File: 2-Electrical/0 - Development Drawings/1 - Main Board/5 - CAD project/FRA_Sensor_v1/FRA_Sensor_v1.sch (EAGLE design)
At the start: 213 parts, among them IC1 CP2101, IC2 ADS1115IDGSR, IC3 P82B715DR, IC4 ADS1115IDGSR, IC5 ADS1115IDGSR, IC8 PCA9555PW, IC9 LDK320ADU50R, J2 ETH_CONN, J3 PJ-059A, J5 WM9734TR-ND, J8 1140084168, J9 + G SCL SDA, Q10 FDN306P, Q11 FDN306P, Q12 FDN306P, Q13 FDN306P, Q14 FDN306P, Q15 FDN306P, Q2 FDN306P, Q3 Si2300DS, Q5 FDN306P, Q6 FDN306P, Q7 DNI, Q8 FDN306P, Q9 FDN306P, T1 BC847, T2 BC847, U1 PCA9509DP, U2 ESP-WROOM-32, X1 TB001-500-02BE, Y3 32.768kHz

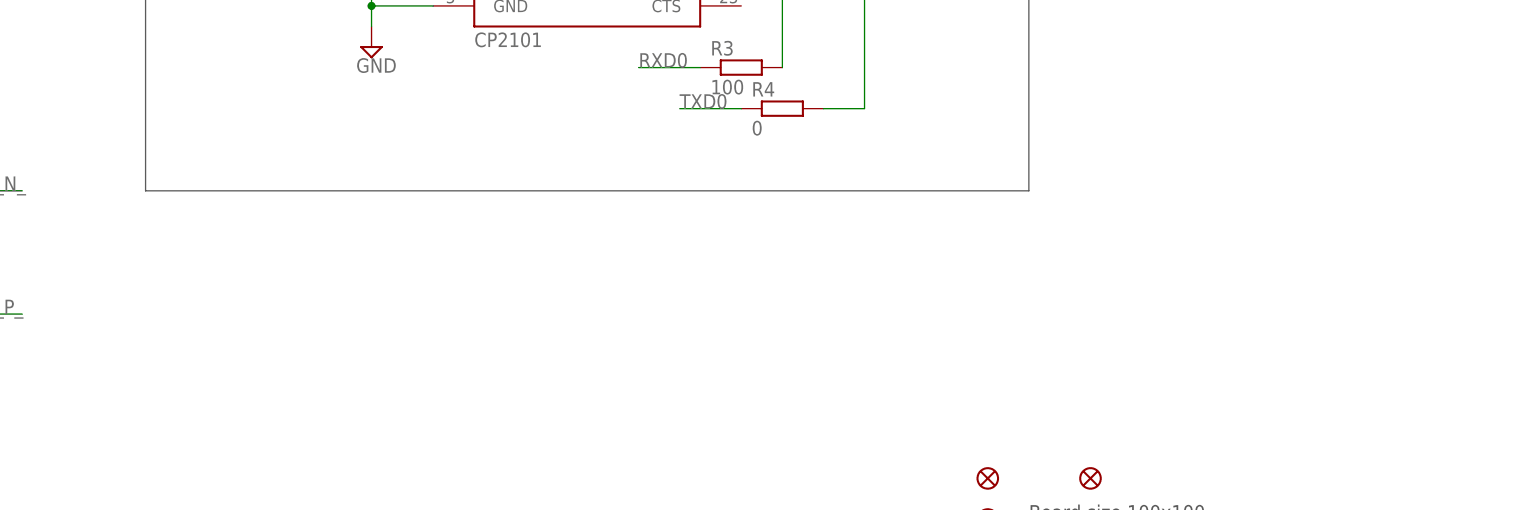
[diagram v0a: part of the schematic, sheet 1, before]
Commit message: fixed network, ADC begin
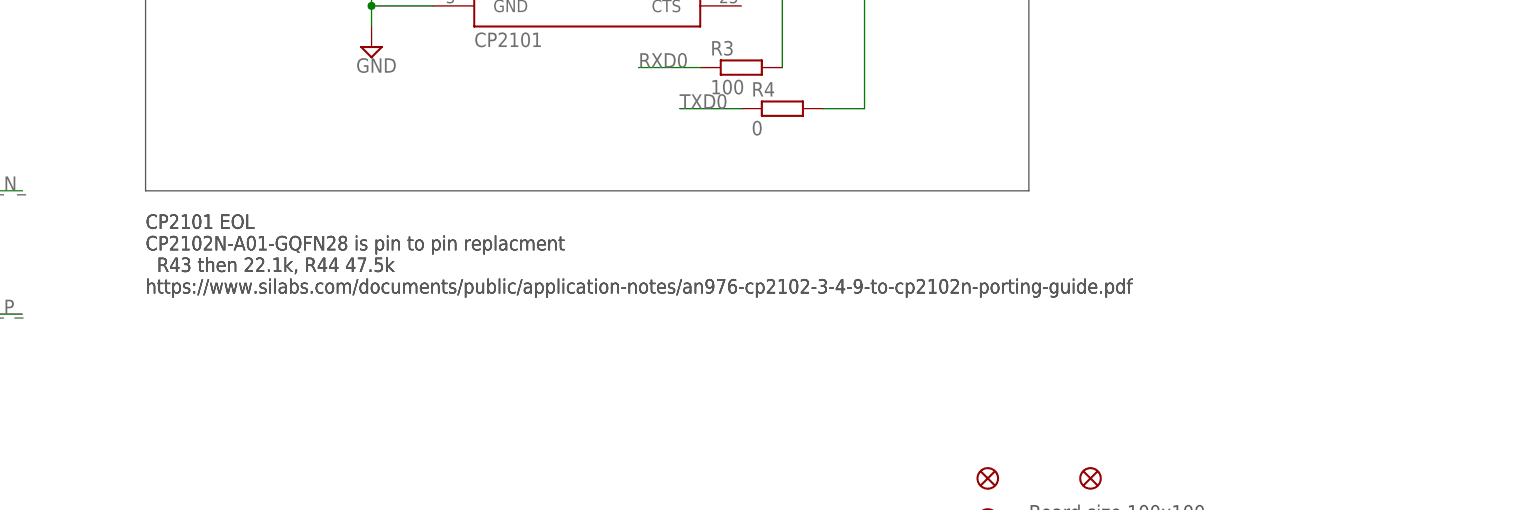
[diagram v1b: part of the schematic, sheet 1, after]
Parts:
- C10: PARTNO (none) -> GRM188R61E106KA73J
- C17: PARTNO (none) -> GRM188R61A106KE69J
- FAN_5V: value FAN -> 2pin; PARTNO 640456-2 -> TSW-102-07-G-S
- J3: PARTNO PJ-031C -> PJ-059A
- J4: value (none) -> DNI
- J5: PARTNO Molex 105133-0001 -> 105133-0001
- J9: value + G SCL SDA -> 4pin
- L2, L3: PARTNO SRN6045TA-1R5Y -> SRP5030CA-1R5M
- LED_HDR: PARTNO 640456-2 -> TSW-102-07-G-S
- U$1, U$4: PARTNO TPS563249DDCR -> TPS563249DDCR
- U$10, U$11, U$12, U$13, U$14, U$15, U$16, U$3, U$8, U$9: PARTNO Wurth 61200621621 -> 61200621621
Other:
- note added: "CP2101 EOL CP2102N-A01-GQFN28 is pin to pin replacment R43 then 22.1k, R44 47.5k https://www.silabs.com/documents/public/application-notes/an976-cp2102-3-4-9-to-cp2102n-porting-guide.pdf"
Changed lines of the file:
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@@
 <attributes>
 <attribute name="CNAME" value="FRA Sensor Unit"/>
-<attribute name="CREVISION" value="02"/>
+<attribute name="CREVISION" value="03"/>
 </attributes>
 <variantdefs>
@@
 <attribute name="PARTNO" value="CES-106-01-T-D"/>
 </part>
-<part name="J4" library="sd-mmc" deviceset="SDCARD" device="">
+<part name="J4" library="sd-mmc" deviceset="SDCARD" device="" value="DNI">
 <attribute name="PARTNO" value="GSD090012SEU"/>
 </part>
 <part name="U$4" library="FRA_eagle_lib" deviceset="TPS5632149DDCR" device="" value="TPS563249DDCR">
-<attribute name="PARTNO" value="TPS563249DDCR"/>
+<attribute name="PARTNO" value="TPS563249DDCR
+"/>
 </part>
 <part name="SUPPLY6" library="supply2" deviceset="GND" device=""/>
@@
 <part name="SUPPLY14" library="supply2" deviceset="GND" device=""/>
 <part name="SUPPLY15" library="supply2" deviceset="GND" device=""/>
-<part name="C10" library="resistor" deviceset="C-EU" device="C0603K" value="10u/25V"/>
+<part name="C10" library="resistor" deviceset="C-EU" device="C0603K" value="10u/25V">
+<attribute name="PARTNO" value="GRM188R61E106KA73J"/>
+</part>
 <part name="SUPPLY21" library="supply2" deviceset="GND" device=""/>
 <part name="SUPPLY22" library="supply2" deviceset="GND" device=""/>
@@
 <part name="SUPPLY30" library="SparkFun-PowerSymbols" deviceset="3.3V" device=""/>
 <part name="L2" library="FRA_eagle_lib" deviceset="SRP5030CA-1R5M" device="" value="SRP5030CA-1R5M">
-<attribute name="PARTNO" value="SRN6045TA-1R5Y"/>
+<attribute name="PARTNO" value="SRP5030CA-1R5M
+"/>
 </part>
 <part name="Q2" library="microbuilder" deviceset="MOSFET-P" device="WIDE" value="FDN306P">
@@
 <part name="SUPPLY49" library="SparkFun-PowerSymbols" deviceset="V_USB" device=""/>
 <part name="U$1" library="FRA_eagle_lib" deviceset="TPS5632149DDCR" device="" value="TPS563249DDCR">
-<attribute name="PARTNO" value="TPS563249DDCR"/>
+<attribute name="PARTNO" value="TPS563249DDCR
+"/>
 </part>
 <part name="SUPPLY11" library="supply2" deviceset="GND" device=""/>
@@
 <part name="SUPPLY55" library="supply2" deviceset="GND" device=""/>
 <part name="SUPPLY60" library="supply2" deviceset="GND" device=""/>
-<part name="C17" library="resistor" deviceset="C-EU" device="C0603K" value="10u"/>
+<part name="C17" library="resistor" deviceset="C-EU" device="C0603K" value="10u">
+<attribute name="PARTNO" value="GRM188R61A106KE69J"/>
+</part>
 <part name="SUPPLY62" library="supply2" deviceset="GND" device=""/>
 <part name="SUPPLY63" library="supply2" deviceset="GND" device=""/>
@@
 </part>
 <part name="L3" library="FRA_eagle_lib" deviceset="SRP5030CA-1R5M" device="" value="SRP5030CA-1R5M">
-<attribute name="PARTNO" value="SRN6045TA-1R5Y"/>
+<attribute name="PARTNO" value="SRP5030CA-1R5M
+"/>
 </part>
 <part name="R53" library="resistor" deviceset="R-EU_" device="R0603" value="100k">
@@
 </part>
 <part name="J5" library="SparkFun-Connectors" deviceset="USB_MICRO-B" device="_FEMALE-SMT-VERT" value="WM9734TR-ND ">
-<attribute name="PARTNO" value="Molex 105133-0001"/>
+<attribute name="PARTNO" value="105133-0001"/>
 </part>
 <part name="SUPPLY68" library="SparkFun-PowerSymbols" deviceset="V_USB" device=""/>
@@
 </part>
 <part name="SUPPLY19" library="supply2" deviceset="GND" device=""/>
-<part name="FAN_5V" library="pinhead" deviceset="PINHD-1X2" device="" value="FAN">
-<attribute name="PARTNO" value="640456-2"/>
+<part name="FAN_5V" library="pinhead" deviceset="PINHD-1X2" device="" value="2pin">
+<attribute name="PARTNO" value="TSW-102-07-G-S"/>
 </part>
 <part name="SUPPLY87" library="SparkFun-PowerSymbols" deviceset="5V" device=""/>
@@
 <part name="SUPPLY121" library="SparkFun-PowerSymbols" deviceset="3.3V" device=""/>
 <part name="U$3" library="FRA_eagle_lib" deviceset="CONN_03X2_WE_61200621621" device="">
-<attribute name="PARTNO" value="Wurth 61200621621"/>
+<attribute name="PARTNO" value="61200621621"/>
 </part>
 <part name="SUPPLY59" library="supply2" deviceset="AGND" device=""/>
@@
 </part>
 <part name="U$8" library="FRA_eagle_lib" deviceset="CONN_03X2_WE_61200621621" device="">
-<attribute name="PARTNO" value="Wurth 61200621621"/>
+<attribute name="PARTNO" value="61200621621"/>
 </part>
 <part name="SUPPLY58" library="supply2" deviceset="AGND" device=""/>
@@
 </part>
 <part name="U$9" library="FRA_eagle_lib" deviceset="CONN_03X2_WE_61200621621" device="">
-<attribute name="PARTNO" value="Wurth 61200621621"/>
+<attribute name="PARTNO" value="61200621621"/>
 </part>
 <part name="SUPPLY108" library="supply2" deviceset="AGND" device=""/>
@@
 </part>
 <part name="U$10" library="FRA_eagle_lib" deviceset="CONN_03X2_WE_61200621621" device="">
-<attribute name="PARTNO" value="Wurth 61200621621"/>
+<attribute name="PARTNO" value="61200621621"/>
 </part>
 <part name="SUPPLY116" library="supply2" deviceset="AGND" device=""/>
@@
 </part>
 <part name="U$11" library="FRA_eagle_lib" deviceset="CONN_03X2_WE_61200621621" device="">
-<attribute name="PARTNO" value="Wurth 61200621621"/>
+<attribute name="PARTNO" value="61200621621"/>
 </part>
 <part name="SUPPLY124" library="supply2" deviceset="AGND" device=""/>
@@
 </part>
 <part name="U$12" library="FRA_eagle_lib" deviceset="CONN_03X2_WE_61200621621" device="">
-<attribute name="PARTNO" value="Wurth 61200621621"/>
+<attribute name="PARTNO" value="61200621621"/>
 </part>
 <part name="SUPPLY126" library="supply2" deviceset="AGND" device=""/>
@@
 <part name="FRAME7" library="SparkFun-Aesthetics" deviceset="FRAME-A4L" device=""/>
 <part name="U$13" library="FRA_eagle_lib" deviceset="CONN_03X2_WE_61200621621" device="">
-<attribute name="PARTNO" value="Wurth 61200621621"/>
+<attribute name="PARTNO" value="61200621621"/>
 </part>
 <part name="SUPPLY70" library="supply2" deviceset="AGND" device=""/>
@@
 </part>
 <part name="U$14" library="FRA_eagle_lib" deviceset="CONN_03X2_WE_61200621621" device="">
-<attribute name="PARTNO" value="Wurth 61200621621"/>
+<attribute name="PARTNO" value="61200621621"/>
 </part>
 <part name="SUPPLY85" library="supply2" deviceset="AGND" device=""/>
@@
 </part>
 <part name="U$15" library="FRA_eagle_lib" deviceset="CONN_03X2_WE_61200621621" device="">
-<attribute name="PARTNO" value="Wurth 61200621621"/>
+<attribute name="PARTNO" value="61200621621"/>
 </part>
 <part name="SUPPLY129" library="supply2" deviceset="AGND" device=""/>
@@
 </part>
 <part name="U$16" library="FRA_eagle_lib" deviceset="CONN_03X2_WE_61200621621" device="">
-<attribute name="PARTNO" value="Wurth 61200621621"/>
+<attribute name="PARTNO" value="61200621621"/>
 </part>
 <part name="SUPPLY131" library="supply2" deviceset="AGND" device=""/>
@@
 </part>
 <part name="SUPPLY66" library="supply2" deviceset="AGND" device=""/>
-<part name="J9" library="pinhead" deviceset="PINHD-1X4" device="" value="+  G  SCL SDA">
+<part name="J9" library="pinhead" deviceset="PINHD-1X4" device="" value="4pin">
 <attribute name="PARTNO" value="61300411121"/>
 </part>
@@
 <part name="SUPPLY96" library="supply2" deviceset="+5V/1" device="" value="5V_F"/>
 <part name="J3" library="FRA_eagle_lib" deviceset="PJ-059A" device="">
-<attribute name="PARTNO" value="PJ-031C"/>
+<attribute name="PARTNO" value="PJ-059A "/>
 </part>
 <part name="FB10" library="microbuilder" deviceset="FERRITE" device="">
@@
 <part name="SUPPLY132" library="SparkFun-PowerSymbols" deviceset="5V" device=""/>
 <part name="LED_HDR" library="pinhead" deviceset="PINHD-1X2" device="" value="2pin">
-<attribute name="PARTNO" value="640456-2"/>
+<attribute name="PARTNO" value="TSW-102-07-G-S"/>
 </part>
 </parts>
@@
 <text x="58.42" y="86.36" size="1.778" layer="97">Molex
 105133-0001</text>
+<text x="142.24" y="55.88" size="1.778" layer="97">CP2101 EOL
+CP2102N-A01-GQFN28 is pin to pin replacment
+  R43 then 22.1k, R44 47.5k
+https://www.silabs.com/documents/public/application-notes/an976-cp2102-3-4-9-to-cp2102n-porting-guide.pdf</text>
+<text x="142.24" y="55.88" size="1.778" layer="97">CP2101 EOL
+CP2102N-A01-GQFN28 is pin to pin replacment
+  R43 then 22.1k, R44 47.5k
+https://www.silabs.com/documents/public/application-notes/an976-cp2102-3-4-9-to-cp2102n-porting-guide.pdf</text>
 </plain>
 <instances>
@@
 <instance part="SUPPLY14" gate="GND" x="101.6" y="127"/>
 <instance part="SUPPLY15" gate="GND" x="88.9" y="127"/>
-<instance part="C10" gate="G$1" x="160.02" y="119.38"/>
+<instance part="C10" gate="G$1" x="160.02" y="119.38">
+<attribute name="PARTNO" x="160.02" y="119.38" size="1.778" layer="96" display="off"/>
+</instance>
 <instance part="SUPPLY21" gate="GND" x="160.02" y="111.76"/>
 <instance part="SUPPLY22" gate="GND" x="170.18" y="111.76"/>
@@
 <instance part="SUPPLY55" gate="GND" x="101.6" y="55.88"/>
 <instance part="SUPPLY60" gate="GND" x="88.9" y="55.88"/>
-<instance part="C17" gate="G$1" x="160.02" y="48.26"/>
+<instance part="C17" gate="G$1" x="160.02" y="48.26">
+<attribute name="PARTNO" x="160.02" y="48.26" size="1.778" layer="96" display="off"/>
+</instance>
 <instance part="SUPPLY62" gate="GND" x="160.02" y="40.64"/>
 <instance part="SUPPLY63" gate="GND" x="170.18" y="40.64"/>

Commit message: sch main final touches
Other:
- note added: "Man. PN may be wrong (TH not SMT)"
- note added: "place on BOT in schematics. placed on top in assembly"
- note removed: "place on BOT"
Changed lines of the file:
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@@
 </part>
 <part name="U$4" library="FRA_eagle_lib" deviceset="TPS5632149DDCR" device="" value="TPS563249DDCR">
-<attribute name="PARTNO" value="TPS563249DDCR
-"/>
+<attribute name="PARTNO" value="TPS563249DDCR "/>
 </part>
 <part name="SUPPLY6" library="supply2" deviceset="GND" device=""/>
@@
 <part name="SUPPLY30" library="SparkFun-PowerSymbols" deviceset="3.3V" device=""/>
 <part name="L2" library="FRA_eagle_lib" deviceset="SRP5030CA-1R5M" device="" value="SRP5030CA-1R5M">
-<attribute name="PARTNO" value="SRP5030CA-1R5M
-"/>
+<attribute name="PARTNO" value="SRP5030CA-1R5M "/>
 </part>
 <part name="Q2" library="microbuilder" deviceset="MOSFET-P" device="WIDE" value="FDN306P">
@@
 <part name="SUPPLY49" library="SparkFun-PowerSymbols" deviceset="V_USB" device=""/>
 <part name="U$1" library="FRA_eagle_lib" deviceset="TPS5632149DDCR" device="" value="TPS563249DDCR">
-<attribute name="PARTNO" value="TPS563249DDCR
-"/>
+<attribute name="PARTNO" value="TPS563249DDCR "/>
 </part>
 <part name="SUPPLY11" library="supply2" deviceset="GND" device=""/>
@@
 </part>
 <part name="L3" library="FRA_eagle_lib" deviceset="SRP5030CA-1R5M" device="" value="SRP5030CA-1R5M">
-<attribute name="PARTNO" value="SRP5030CA-1R5M
-"/>
+<attribute name="PARTNO" value="SRP5030CA-1R5M "/>
 </part>
 <part name="R53" library="resistor" deviceset="R-EU_" device="R0603" value="100k">
@@
 <text x="35.56" y="134.62" size="1.778" layer="97">JTAG connection verified</text>
 <text x="63.5" y="7.62" size="1.778" layer="97">IO34-39 only INPUT</text>
-<text x="180.34" y="73.66" size="1.778" layer="97">place on BOT</text>
+<text x="162.56" y="73.66" size="1.778" layer="97">place on BOT in schematics.
+placed on top in assembly</text>
 <text x="182.88" y="48.26" size="1.778" layer="97">female</text>
 <text x="12.7" y="50.8" size="1.778" layer="97">RTC DNI</text>
@@
 <text x="73.66" y="91.44" size="1.778" layer="97">RTC DNI</text>
 <text x="76.2" y="73.66" size="1.778" layer="97">IO2 must float or LOW</text>
+<text x="22.86" y="170.18" size="1.778" layer="97">Man. PN may be wrong (TH not SMT)</text>
 </plain>
 <instances>

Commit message: BOM updates, labview
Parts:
- C16: PARTNO C0603C102M5RACTU -> CC0603KRX7R8BB104
- C29, C30: value 22p -> DNI
- JTAG1: value (none) -> DNI
- R35: PARTNO CRCW0603330RFKEAC -> CRCW06030000Z0EAC
- R81, R82: PARTNO CRGCQ0603F2K2 -> RCS06032K20JNEA
- S1: PARTNO B3F-3120 -> FSMRA5JH
- U$2: value HEADER_3X6P_ESPPROG -> DNI
- Y3: value 32.768kHz -> DNI
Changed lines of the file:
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@@
 </part>
 <part name="C16" library="resistor" deviceset="C-EU" device="C0603K" value="100n">
-<attribute name="PARTNO" value="C0603C102M5RACTU"/>
+<attribute name="PARTNO" value="CC0603KRX7R8BB104"/>
 </part>
 <part name="SUPPLY26" library="supply2" deviceset="GND" device=""/>
@@
 </part>
 <part name="SUPPLY45" library="supply2" deviceset="GND" device=""/>
-<part name="Y3" library="SparkFun-Clocks" deviceset="CRYSTAL-32.768KHZ" device="SMD-3.2X1.5" value="32.768kHz">
+<part name="Y3" library="SparkFun-Clocks" deviceset="CRYSTAL-32.768KHZ" device="SMD-3.2X1.5" value="DNI">
 <attribute name="PARTNO" value="FC-135 32.7680KA-A3"/>
 </part>
-<part name="C29" library="resistor" deviceset="C-EU" device="C0402" value="22p">
+<part name="C29" library="resistor" deviceset="C-EU" device="C0402" value="DNI">
 <attribute name="PARTNO" value="C0402C220J5GAC7411"/>
 </part>
-<part name="C30" library="resistor" deviceset="C-EU" device="C0402" value="22p">
+<part name="C30" library="resistor" deviceset="C-EU" device="C0402" value="DNI">
 <attribute name="PARTNO" value="C0402C220J5GAC7411"/>
 </part>
@@
 <attribute name="PARTNO" value="PESD1CAN-UX"/>
 </part>
-<part name="JTAG1" library="microbuilder" deviceset="JTAG-CORTEXM3" device="">
+<part name="JTAG1" library="microbuilder" deviceset="JTAG-CORTEXM3" device="" value="DNI">
 <attribute name="PARTNO" value="M50-3600542R"/>
 </part>
-<part name="U$2" library="FRA_eagle_lib" deviceset="HEADER_3X6P_ESPPROG" device="">
+<part name="U$2" library="FRA_eagle_lib" deviceset="HEADER_3X6P_ESPPROG" device="" value="DNI">
 <attribute name="PARTNO" value="HTMS-103-03-T-D-SM"/>
 </part>
@@
 <part name="SUPPLY99" library="supply2" deviceset="GND" device=""/>
 <part name="S1" library="adafruit" deviceset="31-XX" device="">
-<attribute name="PARTNO" value="B3F-3120"/>
+<attribute name="PARTNO" value="FSMRA5JH"/>
 </part>
 <part name="SUPPLY100" library="SparkFun-PowerSymbols" deviceset="3.3V" device=""/>
@@
 <part name="SUPPLY90" library="supply2" deviceset="+5V/1" device="" value="5V_F"/>
 <part name="R81" library="resistor" deviceset="R-EU_" device="R0603" value="2k2">
-<attribute name="PARTNO" value="CRGCQ0603F2K2"/>
+<attribute name="PARTNO" value="RCS06032K20JNEA"/>
 </part>
 <part name="R82" library="resistor" deviceset="R-EU_" device="R0603" value="2k2">
-<attribute name="PARTNO" value="CRGCQ0603F2K2"/>
+<attribute name="PARTNO" value="RCS06032K20JNEA"/>
 </part>
 <part name="SUPPLY101" library="supply2" deviceset="+5V/1" device="" value="5V_F"/>
@@
 <part name="SUPPLY98" library="supply2" deviceset="+5V/1" device="" value="5V_F"/>
 <part name="R35" library="resistor" deviceset="R-EU_" device="R0603" value="0">
-<attribute name="PARTNO" value="CRCW0603330RFKEAC"/>
+<attribute name="PARTNO" value="CRCW06030000Z0EAC"/>
 </part>
 <part name="R36" library="resistor" deviceset="R-EU_" device="R0603" value="DNI">
@@
 <text x="205.74" y="170.18" size="1.778" layer="97">MicroSD slot</text>
 <text x="223.52" y="91.44" size="1.778" layer="97">SD slot</text>
-<text x="35.56" y="134.62" size="1.778" layer="97">JTAG connection verified</text>
+<text x="35.56" y="132.08" size="1.778" layer="97">JTAG connection verified</text>
 <text x="63.5" y="7.62" size="1.778" layer="97">IO34-39 only INPUT</text>
 <text x="162.56" y="73.66" size="1.778" layer="97">place on BOT in schematics.
